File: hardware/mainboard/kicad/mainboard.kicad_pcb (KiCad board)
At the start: 4 copper layers, 54 x 120 mm, 166 parts, among them J1 XT30PW-M, J10 J_PYRO2, J11 J_GPS, J12 J_QWIIC, J13 J_CAM, J14 J_LED, J15 J_STACK, J16 J_SERVO4, J17 J_CHG1, J18 J_CHG2, J19 J_PYRO3, J2 J_BAT1, J20 J_PYRO4, J3 J_SW, J4 J_ARM, J5 J_SERVO1, J6 J_SERVO2, J7 J_SERVO3, J8 J_MOT, J9 J_PYRO1, Q1 AO3401A, Q2 AO3401A, Q3 AO3400A, Q4 AO3400A, Q5 AO3400A, Q6 AO3401A, Q7 AO3401A, Q8 AO3400A, Q9 AO3400A, U10 E22-400T22S, U11 MCP73831T-2ACI/OT, U12 74HC138PW, U13 74HC4051PW, U14 AP2112K-3.3TRG1, U15 BMP390, U2 TPS63070RNMR, U3 AP2112K-3.3TRG1, U4 ICM-42688-P, U5 BMP390, U6 INA239AIDGSR, U7 DRV8833PWPR, U8 SN74LV1T34DBVR

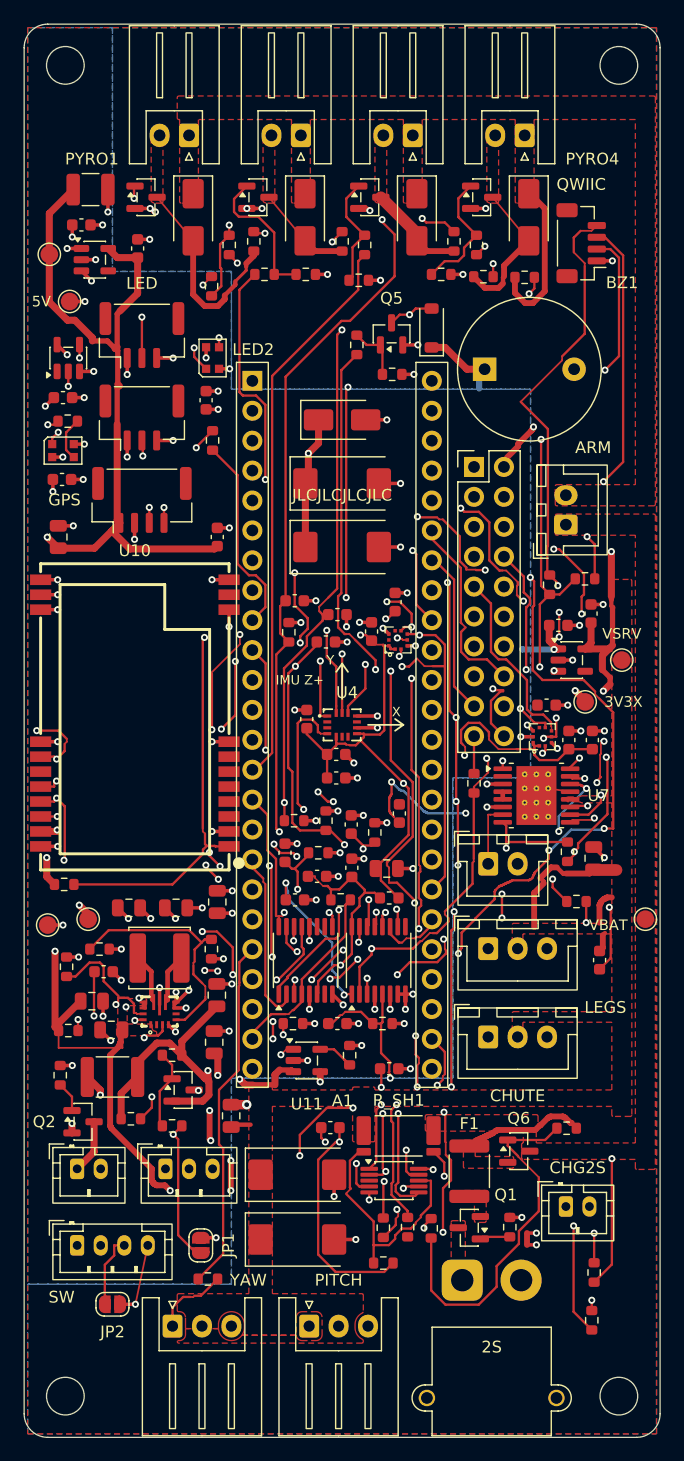
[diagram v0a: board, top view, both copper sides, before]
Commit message: Generator rev B1: Strompfade abgeriegelt, 2S-Kette und DRV8833-Kondensatoren neu platziert; neuer Lauf DRC 0/18
- add_corridor_spines(): 0,2 mm Sperrfläche auf der Mittellinie jedes Strompfads (keine Bahnen,
  keine Vias); die geschrumpfte Sperre aus carve_corridors() verschwand bei schmalen Pfaden, und
  Freerouting schnitt VBAT_PROT über F1 und den VM-Stich des DRV8833 durch.
- Q6 0,8 mm nach rechts, festes Via für sein Gate (ESCAPES); R2 und R4 fest unter Q6 mit eigenen
  VBAT2_F-Pfaden; J18 mit VBAT2_RAW-Pfad zum XT30; VSERVO-Schiene bis J_STACK Pin 5/6.
- C35, C36, C37, C38 fest an U7 bzw. an der VSERVO-Schiene statt 8 bis 14 mm entfernt.
- Ergebnis ./make.sh pcb: 0 DRC-Fehler, 18 offen (vorher 21), andere Stellen als vorher; die
  2S-Kette, J_STACK-VSERVO, U7_VINT, SEL2, CS_EXT0/1 und LORA_M1 sind jetzt verbunden.
  Der Handstand mit 14 offenen liegt in 93a348c.

Co-Authored-By: Claude Opus 5.5 <noreply@anthropic.com>
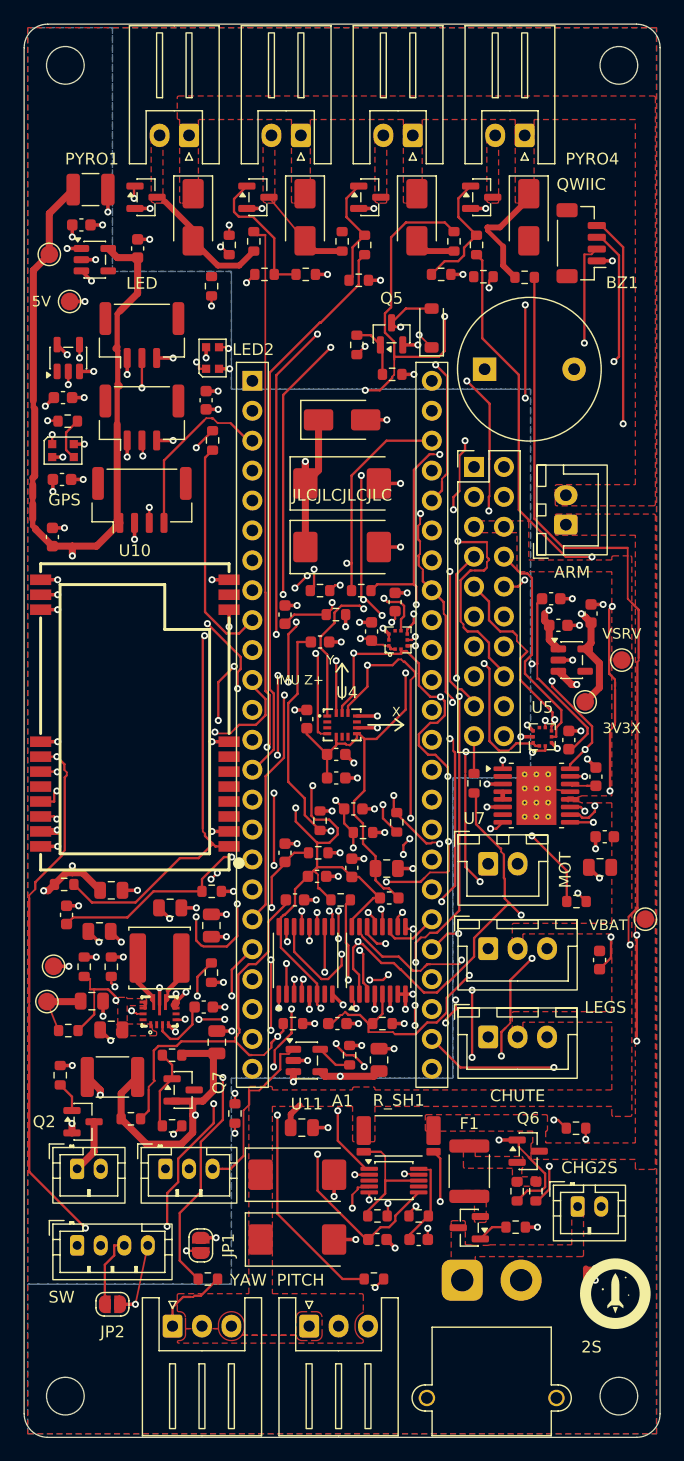
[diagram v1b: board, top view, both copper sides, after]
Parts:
- moved C43 34.3 mm to (103.6, 125.6), turned to 90 degrees
- moved R25 33.4 mm to (117.9, 142.5)
- moved C33 30.3 mm to (107.4, 123.5), turned to 0 degrees
- moved R21 19.5 mm to (125.1, 98.1), turned to 0 degrees
- moved R20 19.0 mm to (128.6, 98.1)
- moved R24 18.8 mm to (129.7, 156.6), turned to 0 degrees
- moved C38 17.0 mm to (148.6, 113.9)
- moved R3 15.0 mm to (146.9, 143.8), turned to 0 degrees
- moved R27 14.7 mm to (131.6, 117.8)
- moved C3 14.5 mm to (130.0, 153.2)
- moved C8 14.1 mm to (130.1, 137.9)
- moved C34 14.0 mm to (102.4, 93.5)
- moved C30 12.5 mm to (144.8, 98.8), turned to 0 degrees
- moved C36 12.2 mm to (149.3, 119.0), turned to 180 degrees
- moved C2 12.1 mm to (133.5, 153.2)
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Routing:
- net CS_EXT0: track 0.00 -> 111.7 mm, vias 0 -> 12
- net LORA_TXD: track 76.6 -> 182.5 mm, vias 5 -> 6
- net LORA_RXD: track 91.7 -> 0.00 mm, vias 7 -> 0
- net PYRO3_SENSE: track 79.1 -> 162.1 mm
- net 3V3: track 164.9 -> 234.7 mm, vias 9 -> 12
- net CS_EXT2: track 67.2 -> 1.44 mm, vias 5 -> 1
- net SERVO_CHUTE: track 112.2 -> 47.8 mm, vias 1 -> 4
- net CS_BARO: track 102.5 -> 42.4 mm, vias 10 -> 4
- net PYRO1_SENSE: track 121.9 -> 65.0 mm, vias 5 -> 4
- net VSYS_IN: track 58.9 -> 5.53 mm, vias 10 -> 0
- net CS_EXT1: track 0.00 -> 52.5 mm, vias 0 -> 5
- net MOT_IN2: track 107.0 -> 58.5 mm
- net BUZZER: track 56.3 -> 97.3 mm, vias 3 -> 2
- net LORA_M1: track 0.00 -> 39.1 mm, vias 0 -> 3
- net PYRO4_FIRE: track 56.5 -> 95.6 mm, vias 1 -> 5
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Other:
- board text added: "MOT"

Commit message: Nacharbeit Lauf 1: 10 Verbindungen per Planer und von Hand (GND an U6/U2, VSYS_IN, 5V_SYS, GND_PWR, VSERVO C37, PYRO2_SENSE); DRC 0/8
Co-Authored-By: Claude Opus 5.5 <noreply@anthropic.com>
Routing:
- net PYRO2_SENSE: track 35.4 -> 76.7 mm, vias 2 -> 8
- net VSYS_IN: track 5.53 -> 17.1 mm, vias 0 -> 2
- net GND: track 103.8 -> 107.5 mm, vias 88 -> 89
- net 5V_SYS: track 44.5 -> 48.0 mm, vias 22 -> 23
- net GND_PWR: track 29.9 -> 33.2 mm, vias 18 -> 20
- net VSERVO: track 2.23 -> 3.28 mm

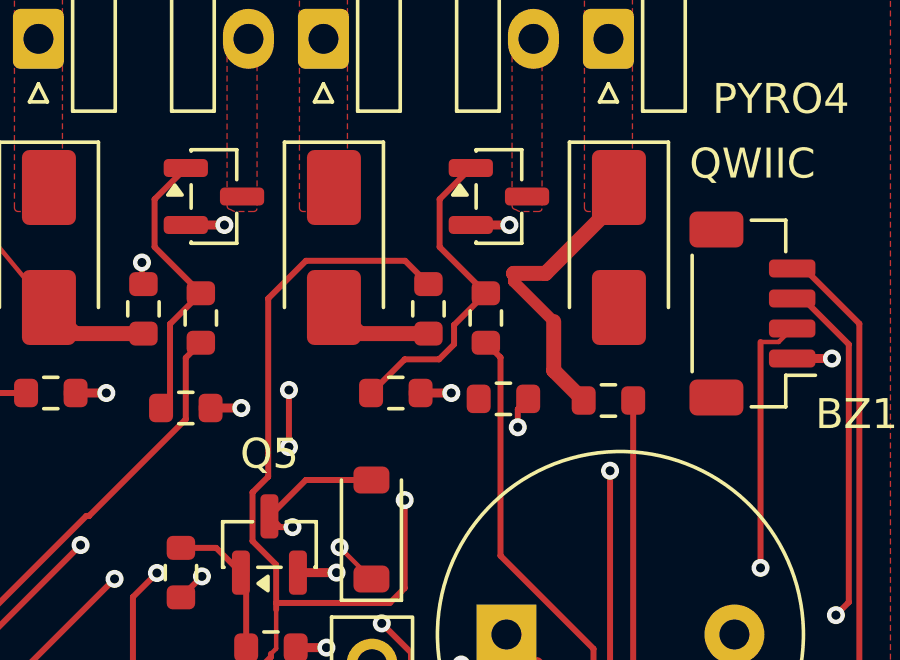
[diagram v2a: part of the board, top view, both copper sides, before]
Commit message: Nacharbeit: PYRO3_NEG (Messleitung über In2) und PYRO4_NEG (VBAT_ARMED-Abgriff rechts um D6, R44 gedreht); DRC 0/5
Co-Authored-By: Claude Opus 5.5 <noreply@anthropic.com>
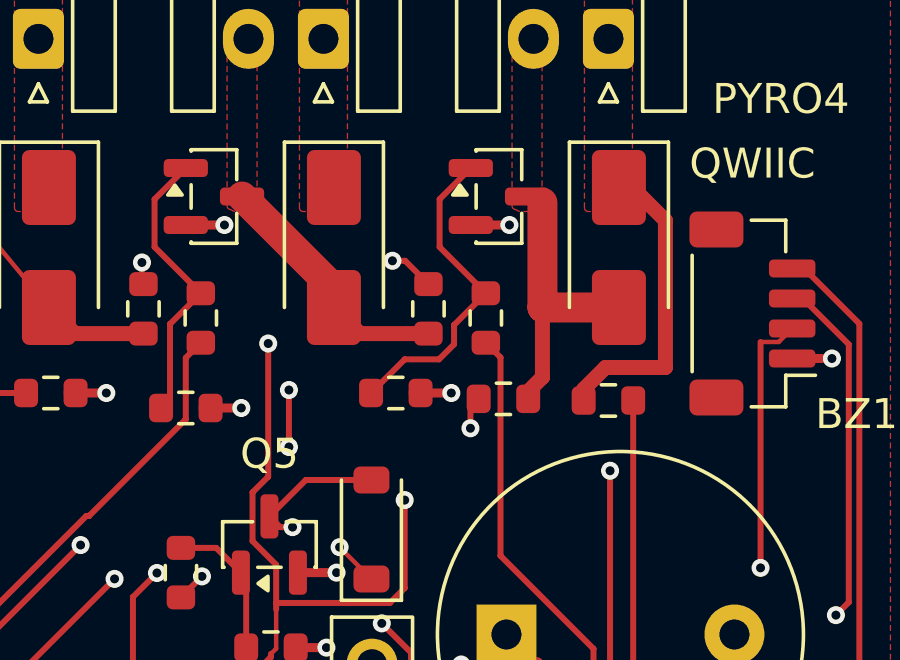
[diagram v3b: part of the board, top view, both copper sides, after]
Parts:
- turned R44 to 180 degrees
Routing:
- net PYRO4_NEG: track 0.00 -> 8.84 mm
- net PYRO3_NEG: track 3.51 -> 8.48 mm
- net PYRO4_SENSE: track 103.4 -> 101.8 mm
- net PYRO3_SENSE: track 162.1 -> 161.2 mm, vias 4 -> 6
- net VBAT_ARMED: track 9.23 -> 9.86 mm
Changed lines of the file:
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@@
 	(footprint "Resistor_SMD:R_0603_1608Metric"
 		(layer "F.Cu")
-		(at 139 71.445)
+		(at 139 71.445 180)
 		(descr "Resistor SMD 0603 (1608 Metric), square (rectangular) end terminal, IPC-7351 nominal, (Body size source: IPC-SM-782 page 72, https://www.pcb-3d.com/wordpress/wp-content/uploads/ipc-sm-782a_amendment_1_and_2.pdf)")
 		(tags "resistor")
 		(property "Reference" "R44"
-			(at 0 -1.43 0)
+			(at 0 -1.43 180)
 			(layer "F.Fab")
 			(effects
@@
 		)
 		(property "Value" "100k"
-			(at 0 1.43 0)
+			(at 0 1.43 180)
 			(layer "F.Fab")
 			(effects
@@
 		)
 		(property "Datasheet" ""
-			(at 0 0 0)
+			(at 0 0 180)
 			(layer "F.Fab")
 			(hide yes)
@@
 		)
 		(property "Description" "Durchgangspruefung, ueber den Analogmux"
-			(at 0 0 0)
+			(at 0 0 180)
 			(layer "F.Fab")
 			(hide yes)
@@
 		)
 		(property "KiLib_Generator" "SMD_2terminal_chip_molded"
-			(at 0 0 0)
+			(at 0 0 180)
 			(layer "F.SilkS")
 			(hide yes)
@@
 		(duplicate_pad_numbers_are_jumpers no)
 		(fp_line
-			(start -0.237258 -0.5225)
-			(end 0.237258 -0.5225)
+			(start -0.237258 0.5225)
+			(end 0.237258 0.5225)
 			(stroke
 				(width 0.12)
@@
 		)
 		(fp_line
-			(start -0.237258 0.5225)
-			(end 0.237258 0.5225)
+			(start -0.237258 -0.5225)
+			(end 0.237258 -0.5225)
 			(stroke
 				(width 0.12)
@@
 		)
 		(fp_text user "${REFERENCE}"
-			(at 0 0 0)
+			(at 0 0 180)
 			(layer "F.Fab")
 			(effects
@@
 		)
 		(pad "1" smd roundrect
-			(at -0.825 0)
+			(at -0.825 0 180)
 			(size 0.8 0.95)
 			(layers "F.Cu" "F.Mask" "F.Paste")
@@
 		)
 		(pad "2" smd roundrect
-			(at 0.825 0)
+			(at 0.825 0 180)
 			(size 0.8 0.95)
 			(layers "F.Cu" "F.Mask" "F.Paste")
@@
 	)
 	(segment
-		(start 142.5 65.1689)
-		(end 140.4054 67.2635)
+		(start 143.3 64.4)
+		(end 144.4 65.5)
 		(width 0.5)
 		(layer "F.Cu")
@@
 	)
 	(segment
-		(start 139.3385 67.2635)
-		(end 139.3385 67.2636)
+		(start 144.4 65.5)
+		(end 144.4 70.4)
 		(width 0.5)
 		(layer "F.Cu")
@@
 	)
 	(segment
-		(start 140.4054 67.2635)
-		(end 139.3385 67.2635)
+		(start 144.4 70.4)
+		(end 142.4 70.4)
 		(width 0.5)
 		(layer "F.Cu")
@@
 	)
 	(segment
-		(start 139.3385 67.2636)
-		(end 139.3385 67.5301)
-		(width 0.375)
-		(layer "F.Cu")
-		(net "VBAT_ARMED")
-	)
-	(segment
-		(start 140.676 68.8676)
-		(end 140.676 70.501)
-		(width 0.5)
-		(layer "F.Cu")
-		(net "VBAT_ARMED")
-	)
-	(segment
-		(start 140.676 70.501)
+		(start 141.675 71.125)
 		(end 141.675 71.5)
 		(width 0.5)
@@
 	)
 	(segment
-		(start 139.3385 67.5301)
-		(end 140.676 68.8676)
-		(width 0.375)
+		(start 142.4 70.4)
+		(end 141.675 71.125)
+		(width 0.5)
 		(layer "F.Cu")
 		(net "VBAT_ARMED")
@@
 	)
 	(segment
-		(start 132.416 66.8432)
-		(end 131.1589 68.1003)
-		(width 0.2)
-		(layer "F.Cu")
-		(net "PYRO3_SENSE")
-	)
-	(segment
 		(start 122.925 100.1375)
 		(end 125.65 100.1375)
@@
 	)
 	(segment
+		(start 131.158899 69.6)
+		(end 131.158899 74.0397)
+		(width 0.2)
+		(layer "F.Cu")
+		(net "PYRO3_SENSE")
+	)
+	(segment
 		(start 128.6999 127.3769)
 		(end 128.6744 127.3514)
@@
 	)
 	(segment
-		(start 135.7232 66.8432)
-		(end 132.416 66.8432)
+		(start 135.7088 77.7525)
+		(end 135.7088 74.8198)
 		(width 0.2)
 		(layer "F.Cu")
@@
 	)
 	(segment
-		(start 135.7088 77.7525)
-		(end 135.7088 74.8198)
+		(start 135.7232 66.843199)
+		(end 135.3 66.843199)
 		(width 0.2)
 		(layer "F.Cu")
@@
 	)
 	(segment
-		(start 131.1589 68.1003)
-		(end 131.1589 74.0397)
-		(width 0.2)
-		(layer "F.Cu")
-		(net "PYRO3_SENSE")
-	)
-	(segment
 		(start 131.424 78.2489)
 		(end 131.424 78.4691)
@@
 	)
 	(via
+		(at 131.158899 69.6)
+		(size 0.6)
+		(drill 0.3)
+		(layers "F.Cu" "B.Cu")
+		(net "PYRO3_SENSE")
+	)
+	(via
 		(at 135.7088 74.8198)
 		(size 0.6)
@@
 		(net "PYRO3_SENSE")
 	)
+	(via
+		(at 135.3 66.843199)
+		(size 0.6)
+		(drill 0.3)
+		(layers "F.Cu" "B.Cu")
+		(net "PYRO3_SENSE")
+	)
+	(segment
+		(start 135.3 66.843199)
+		(end 132.5421 69.6)
+		(width 0.2)
+		(layer "In2.Cu")
+		(net "PYRO3_SENSE")
+	)
 	(segment
 		(start 128.9657 81.0912)
@@
 	)
 	(segment
+		(start 132.5421 69.6)
+		(end 131.158899 69.6)
+		(width 0.2)
+		(layer "In2.Cu")
+		(net "PYRO3_SENSE")
+	)
+	(segment
 		(start 153.5672 128.1272)
 		(end 153.5672 80.2915)
@@
 	)
 	(segment
+		(start 133.35 67.763)
+		(end 133.35 68.4)
+		(width 1)
+		(layer "F.Cu")
+		(net "PYRO3_NEG")
+	)
+	(segment
+		(start 130.2875 64.7)
+		(end 133.35 67.763)
+		(width 1)
+		(layer "F.Cu")
+		(net "PYRO3_NEG")
+	)
+	(segment
 		(start 133.35 68.4)
 		(end 134.22 69.27)
@@
 	)
 	(segment
-		(start 139.825 71.445)
-		(end 139.4785 71.7915)
-		(width 0.2)
-		(layer "F.Cu")
-		(net "PYRO4_SENSE")
-	)
-	(segment
 		(start 121.4132 79.811)
 		(end 121.4132 101.8207)
@@
 	)
 	(segment
-		(start 139.4785 71.7915)
-		(end 139.4785 72.3915)
-		(width 0.2)
-		(layer "F.Cu")
-		(net "PYRO4_SENSE")
-	)
-	(segment
 		(start 103.6 126.412)
 		(end 103.6 126.4125)
@@
 	)
 	(segment
+		(start 138.175 71.445)
+		(end 137.9 71.72)
+		(width 0.2)
+		(layer "F.Cu")
+		(net "PYRO4_SENSE")
+	)
+	(segment
 		(start 130.425 125.2538)
 		(end 130.3176 125.1464)
@@
 		(net "PYRO4_SENSE")
 	)
+	(segment
+		(start 137.9 71.72)
+		(end 137.9 72.425)
+		(width 0.2)
+		(layer "F.Cu")
+		(net "PYRO4_SENSE")
+	)
 	(via
-		(at 121.4132 101.8207)
+		(at 137.9 72.425)
 		(size 0.6)
 		(drill 0.3)
@@
 	)
 	(via
-		(at 124.9056 76.3186)
+		(at 121.4132 101.8207)
 		(size 0.6)
 		(drill 0.3)
@@
 	)
 	(via
-		(at 130.3176 125.1464)
+		(at 124.9056 76.3186)
 		(size 0.6)
 		(drill 0.3)
@@
 	)
 	(via
-		(at 139.4785 72.3915)
+		(at 130.3176 125.1464)
 		(size 0.6)
 		(drill 0.3)
@@
 	)
 	(segment
-		(start 139.4785 72.3915)
-		(end 128.8327 72.3915)
-		(width 0.2)
+		(start 119.5688 117.0228)
+		(end 119.6714 117.1254)
+		(width 0.15)
 		(layer "In2.Cu")
 		(net "PYRO4_SENSE")
 	)
 	(segment
-		(start 119.5688 117.0228)
-		(end 119.6714 117.1254)
-		(width 0.15)
+		(start 137.9 72.425)
+		(end 137.9 72.3915)
+		(width 0.2)
 		(layer "In2.Cu")
 		(net "PYRO4_SENSE")
@@
 	)
 	(segment
+		(start 137.9 72.3915)
+		(end 128.832699 72.3915)
+		(width 0.2)
+		(layer "In2.Cu")
+		(net "PYRO4_SENSE")
+	)
+	(segment
 		(start 117.5534 105.0247)
 		(end 117.5534 116.8727)
@@
 	)
 	(segment
+		(start 140.3 68.4)
+		(end 140.3 64.9)
+		(width 1)
+		(layer "F.Cu")
+		(net "PYRO4_NEG")
+	)
+	(segment
+		(start 140.3 70.725)
+		(end 139.825 71.2)
+		(width 0.5)
+		(layer "F.Cu")
+		(net "PYRO4_NEG")
+	)
+	(segment
+		(start 142.4 68.4)
+		(end 140.3 68.4)
+		(width 1)
+		(layer "F.Cu")
+		(net "PYRO4_NEG")
+	)
+	(segment
+		(start 139.825 71.2)
+		(end 139.825 71.445)
+		(width 0.5)
+		(layer "F.Cu")
+		(net "PYRO4_NEG")
+	)
+	(segment
+		(start 140.3 68.4)
+		(end 140.3 70.725)
+		(width 0.5)
+		(layer "F.Cu")
+		(net "PYRO4_NEG")
+	)
+	(segment
